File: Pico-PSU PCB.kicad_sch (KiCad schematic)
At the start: 0 parts

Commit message: drafting schematics
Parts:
- added C1: 10u, symbol Device:C_Polarized
- added D1: 1N5819, symbol Device:D_Schottky
- added Q1: BC547, Package_TO_SOT_THT:TO-92_Inline, symbol Transistor_BJT:BC547
- added R1: 10k, symbol Device:R
- added R2: 1k, symbol Device:R
- added U1: LM324, symbol Amplifier_Operational:LM324
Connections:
- new net: Q1.2 (B), U1.7
- new net: Q1.3 (E), R2.1, U1.6 (-)
- new net: C1.1, R1.2, U1.3 (+)
- new net: U1.1, U1.2 (-), U1.5 (+)
- new net +BATT: D1.2 (A)
- new net GND: C1.2, R2.2
- new net VCC: D1.1 (K)

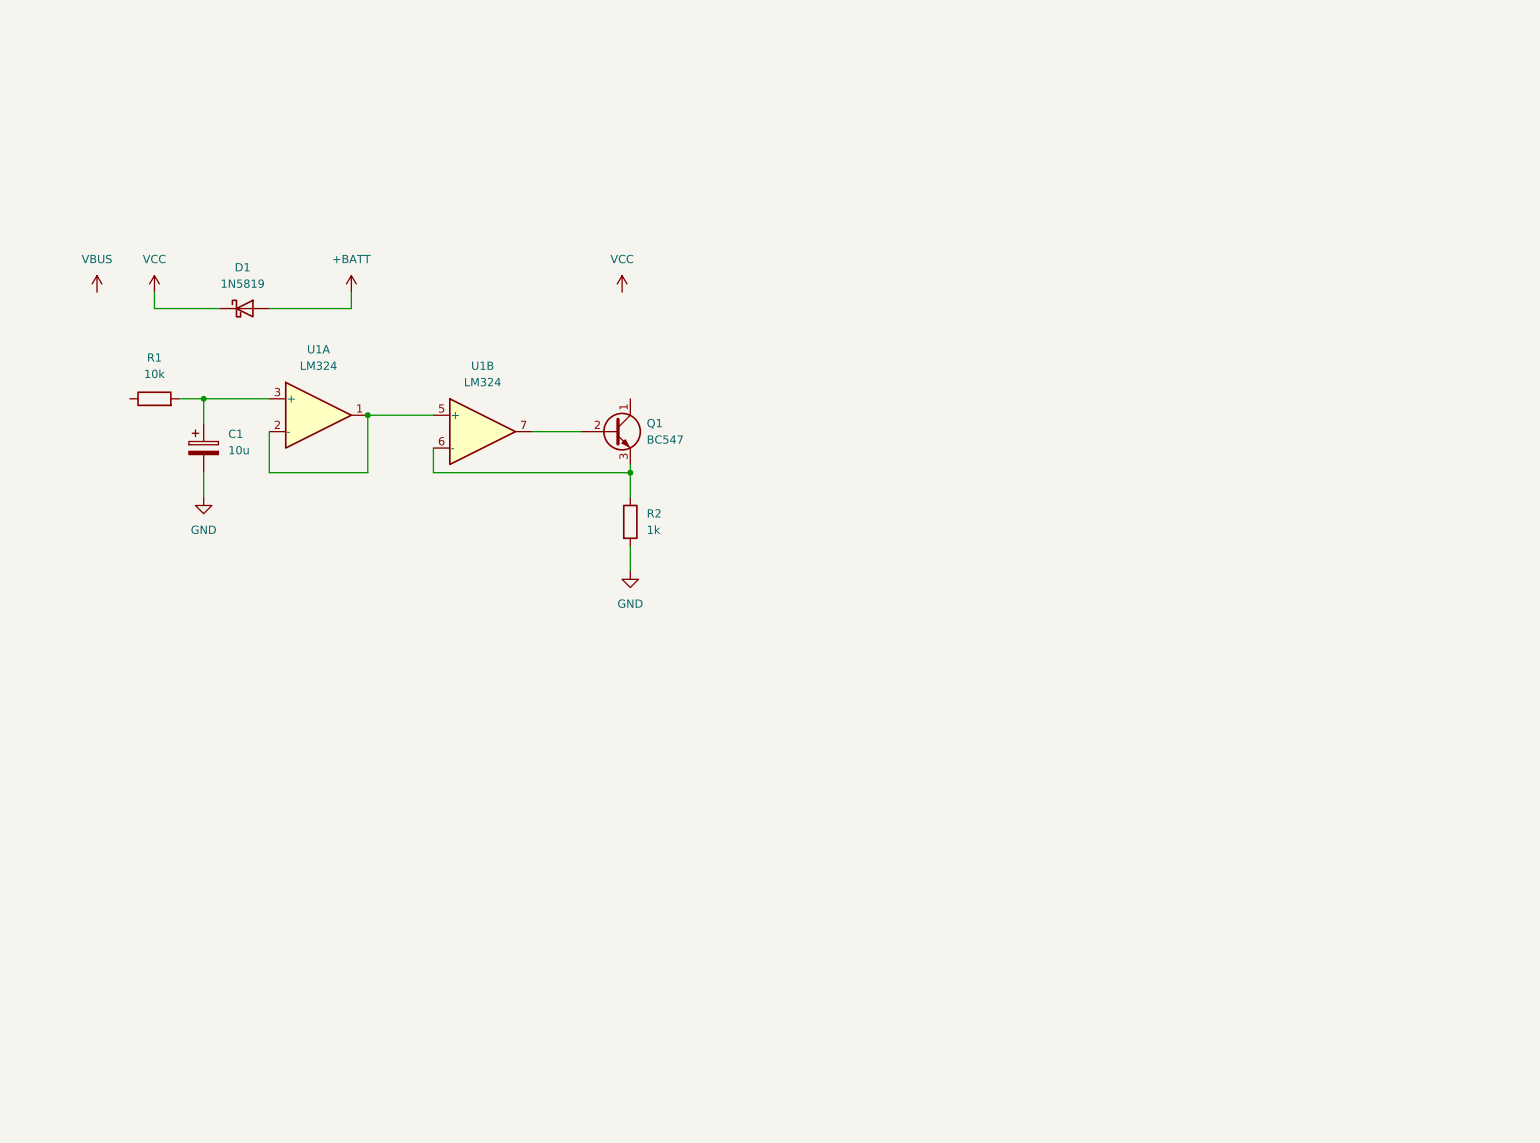
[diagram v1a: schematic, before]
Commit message: updated schema with dual channels
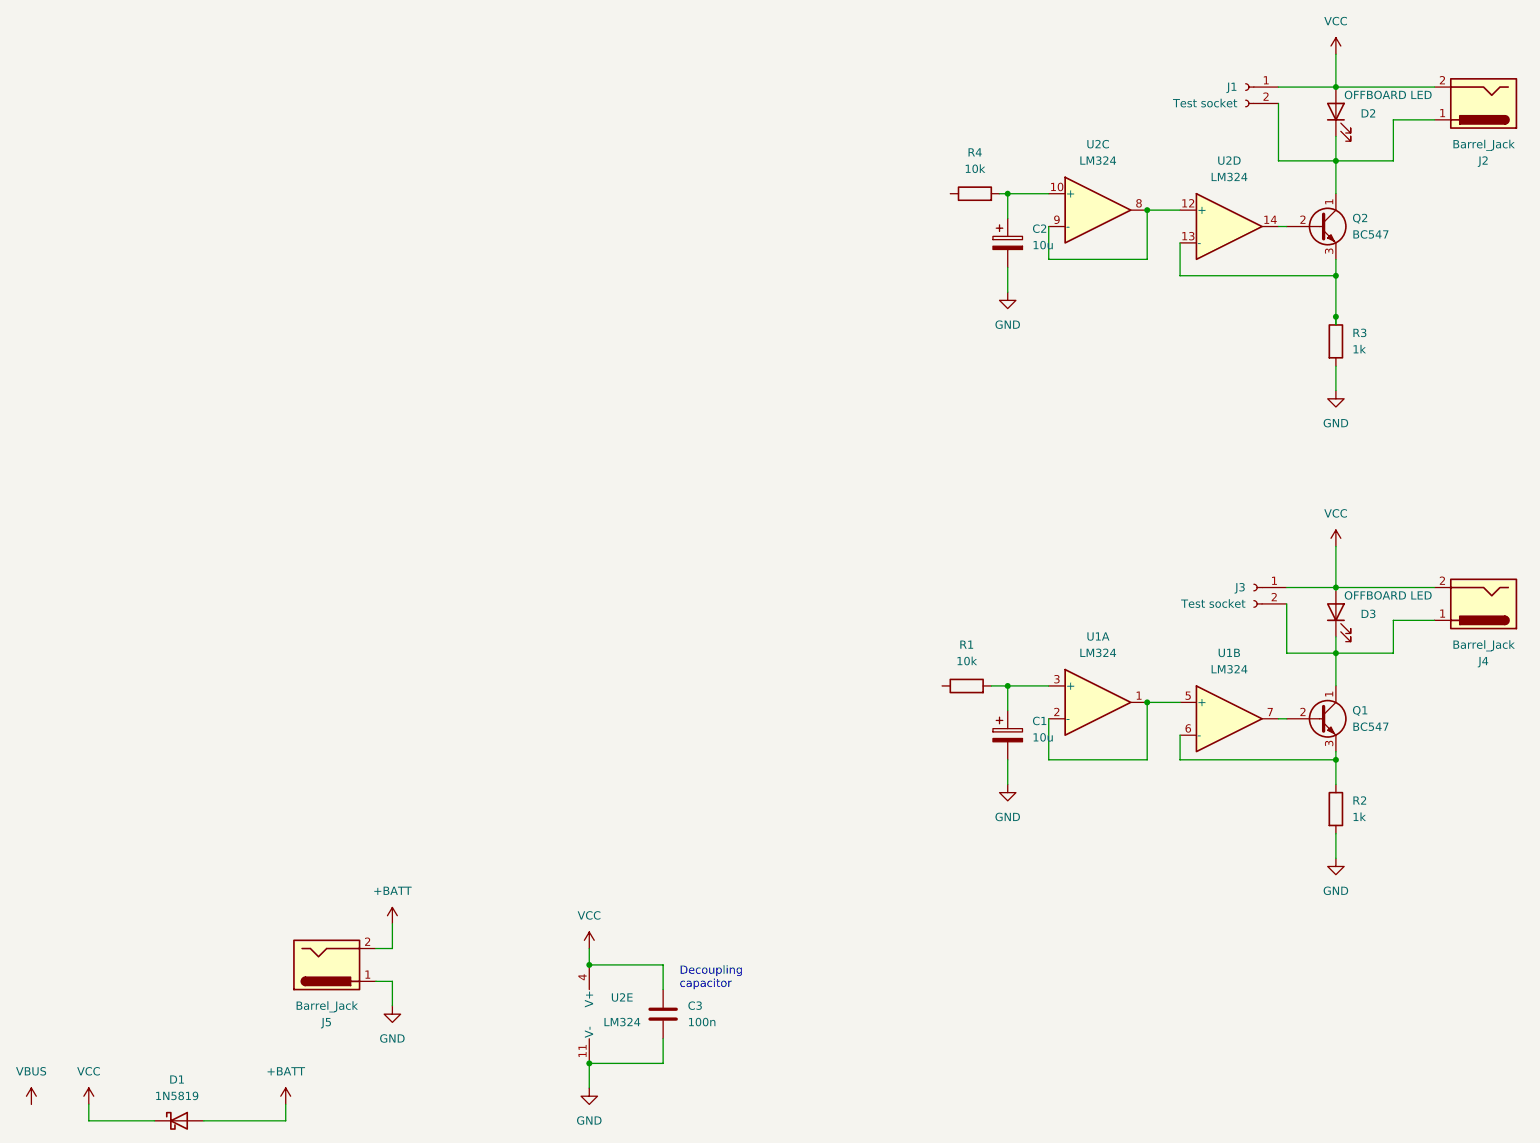
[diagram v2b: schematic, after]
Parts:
- added C2: 10u, symbol Device:C_Polarized
- added C3: 100n, symbol Device:C
- added D2, D3: OFFBOARD LED, symbol Device:LED
- added J1, J3: Test socket, symbol Connector:Conn_01x02_Socket
- added J2, J4, J5: Barrel_Jack, symbol Connector:Barrel_Jack
- added Q2: BC547, Package_TO_SOT_THT:TO-92_Inline, symbol Transistor_BJT:BC547
- added R3: 1k, symbol Device:R
- added R4: 10k, symbol Device:R
- added U2: LM324, symbol Amplifier_Operational:LM324
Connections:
- net +BATT: now also J5.2
- net GND: now also C2.2, C3.2, J5.1, R3.2, U2.11 (V-)
- net VCC: now also C3.1, D2.2 (A), D3.2 (A), J1.1 (Pin_1), J2.2, J3.1 (Pin_1), J4.2, U2.4 (V+)
- net at Q1.1 (C): now also D3.1 (K), J3.2 (Pin_2), J4.1
- new net: U2.12 (+), U2.8, U2.9 (-)
- new net: Q2.3 (E), R3.1, U2.13 (-)
- new net: Q2.2 (B), U2.14
- new net: C2.1, R4.2, U2.10 (+)
- new net: D2.1 (K), J1.2 (Pin_2), J2.1, Q2.1 (C)
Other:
- note added: "Decoupling capacitor"
- title: Programmable constant current power supply -> Dual Programmable constant current power supply
- moved on the sheet: C1, D1, Q1, R1, R2, U1A, U1B
